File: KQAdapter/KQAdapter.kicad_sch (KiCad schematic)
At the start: 3 parts

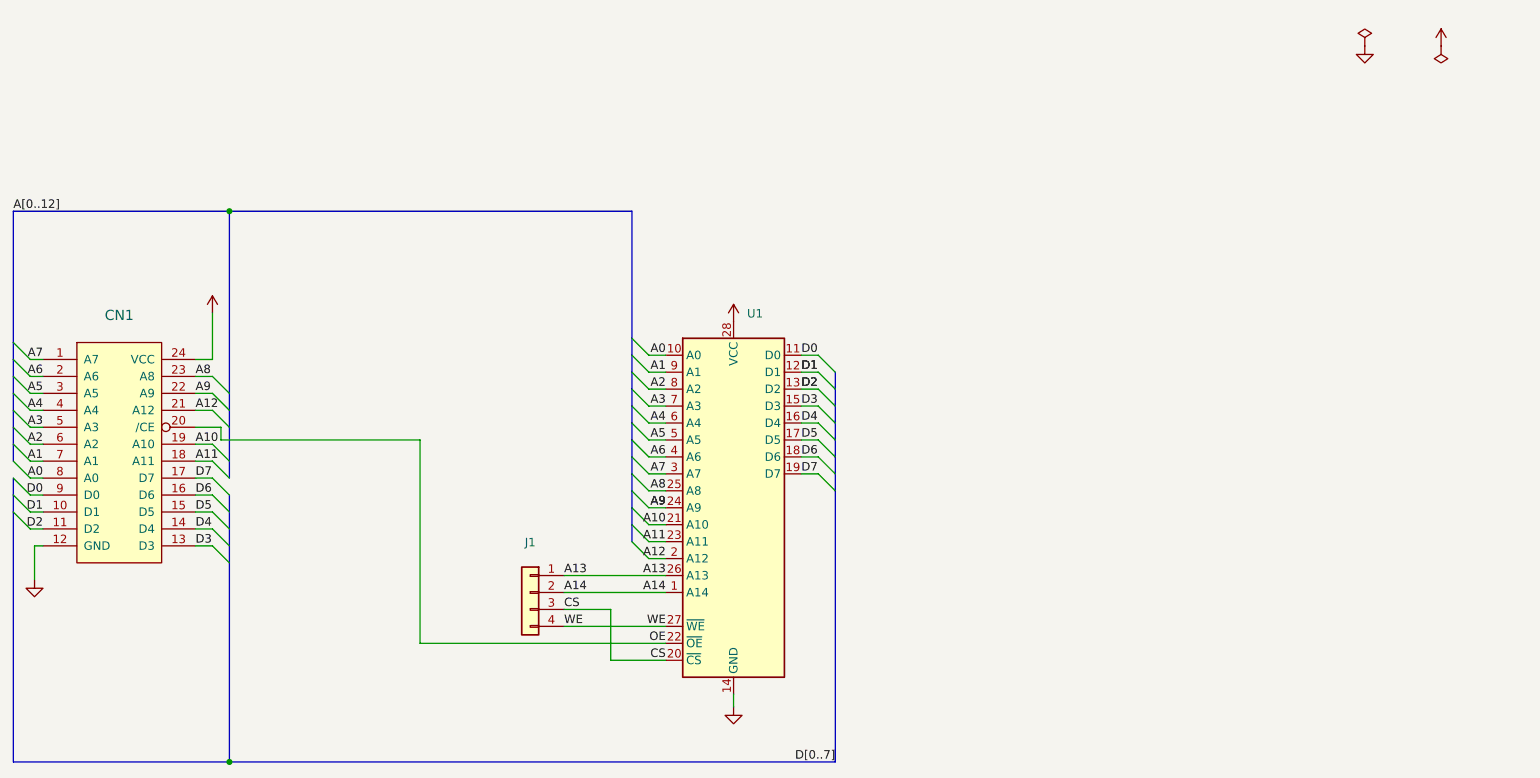
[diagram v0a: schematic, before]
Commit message: Added license information.
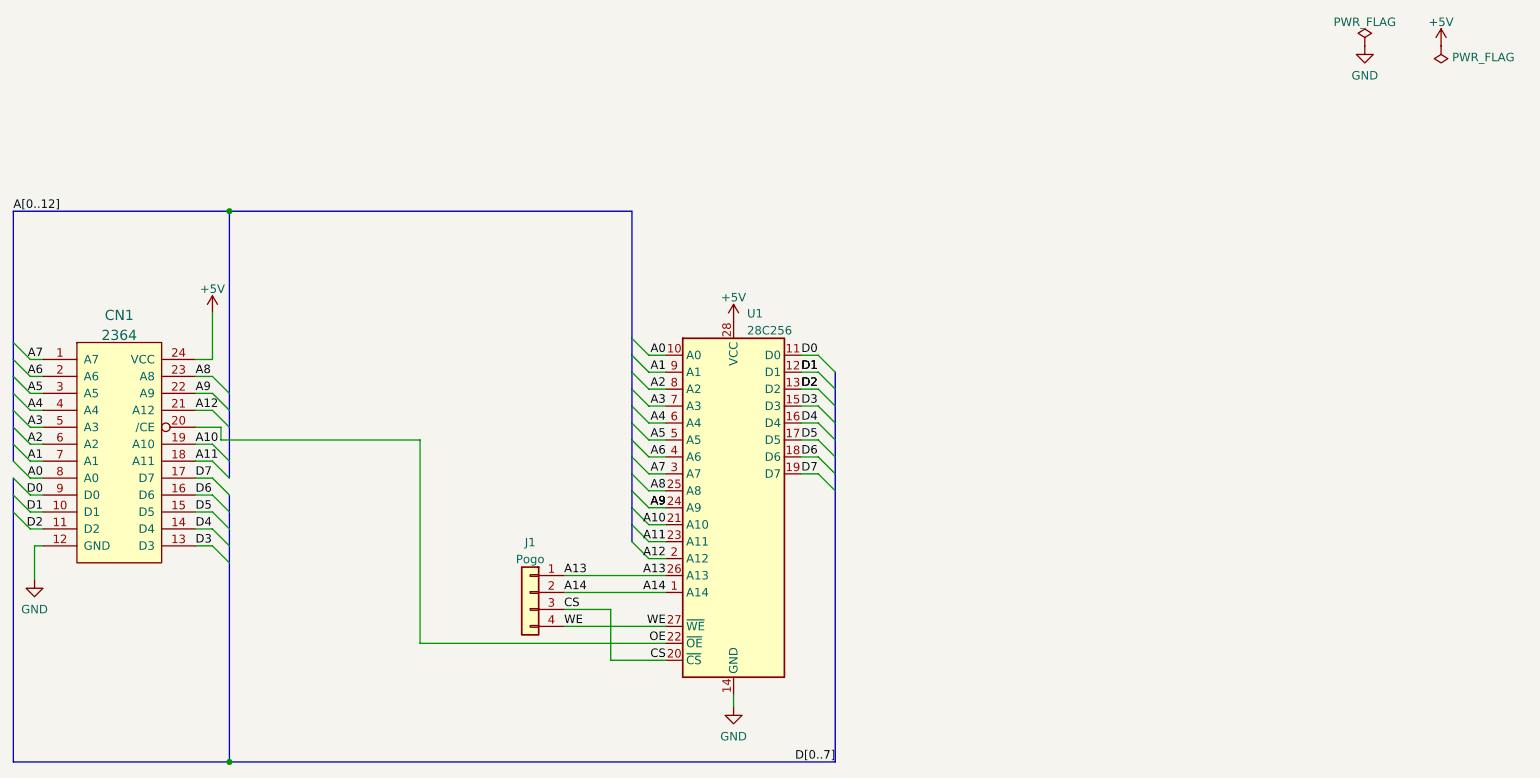
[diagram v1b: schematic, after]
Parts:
- CN1: value (none) -> 2364; footprint (none) -> Package_DIP:DIP-24_W15.24mm_Socket
- J1: value (none) -> Pogo; footprint (none) -> Connector_PinHeader_2.54mm:PinHeader_1x04_P2.54mm_Vertical
- U1: value (none) -> 28C256; footprint (none) -> Package_DIP:DIP-28_W15.24mm
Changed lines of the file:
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@@
   (title_block
     (title "KERNALquattro Adapter")
+    (date "2022-05-02")
     (rev "1")
     (company "www.hackup.net")
+    (comment 1 "Creative Commons Attribution-NonCommercial-ShareAlike 4.0 International License.")
+    (comment 2 "This work is licensed under a")
   )
   (junction (at 85.725 48.26) (diameter 0) (color 0 0 0 0)
@@
       (effects (font (size 1.27 1.27)) hide)
     )
-    (property "Value" "" (id 1) (at 268.986 25.1988 0)
+    (property "Value" "PWR_FLAG" (id 1) (at 268.986 25.1988 0)
       (effects (font (size 1.27 1.27)) (justify right))
     )
@@
       (effects (font (size 1.27 1.27)) hide)
     )
-    (property "Value" "" (id 1) (at 255.905 27.9384 0))
+    (property "Value" "GND" (id 1) (at 255.905 27.9384 0))
     (property "Footprint" "" (id 2) (at 255.905 23.495 0)
       (effects (font (size 1.27 1.27)) hide)
@@
       (effects (font (size 1.27 1.27)) hide)
     )
-    (property "Value" "" (id 1) (at 255.905 19.9192 0))
+    (property "Value" "PWR_FLAG" (id 1) (at 255.905 19.9192 0))
     (property "Footprint" "" (id 2) (at 255.905 23.495 0)
       (effects (font (size 1.27 1.27)) hide)
@@
     (in_bom yes) (on_board yes) (fields_autoplaced)
     (property "Reference" "J1" (id 0) (at 130.81 97.9002 0))
-    (property "Value" "" (id 1) (at 130.81 100.4371 0))
-    (property "Footprint" "" (id 2) (at 130.81 105.41 0)
+    (property "Value" "Pogo" (id 1) (at 130.81 100.4371 0))
+    (property "Footprint" "Connector_PinHeader_2.54mm:PinHeader_1x04_P2.54mm_Vertical" (id 2) (at 130.81 105.41 0)
       (effects (font (size 1.27 1.27)) hide)
     )
@@
       (effects (font (size 1.27 1.27)) hide)
     )
-    (property "Value" "" (id 1) (at 161.29 61.1942 0))
+    (property "Value" "+5V" (id 1) (at 161.29 61.1942 0))
     (property "Footprint" "" (id 2) (at 161.29 64.77 0)
       (effects (font (size 1.27 1.27)) hide)
@@
       (effects (font (size 1.27 1.27)) hide)
     )
-    (property "Value" "" (id 1) (at 161.29 126.9984 0))
+    (property "Value" "GND" (id 1) (at 161.29 126.9984 0))
     (property "Footprint" "" (id 2) (at 161.29 122.555 0)
       (effects (font (size 1.27 1.27)) hide)
@@
       (effects (font (size 1.27 1.27)) hide)
     )
-    (property "Value" "" (id 1) (at 83.185 59.9242 0))
+    (property "Value" "+5V" (id 1) (at 83.185 59.9242 0))
     (property "Footprint" "" (id 2) (at 83.185 63.5 0)
       (effects (font (size 1.27 1.27)) hide)
@@
       (effects (font (size 1.27 1.27)) (justify left))
     )
-    (property "Value" "" (id 1) (at 163.3094 66.1471 0)
+    (property "Value" "28C256" (id 1) (at 163.3094 66.1471 0)
       (effects (font (size 1.27 1.27)) (justify left))
     )
-    (property "Footprint" "" (id 2) (at 161.29 92.71 0)
+    (property "Footprint" "Package_DIP:DIP-28_W15.24mm" (id 2) (at 161.29 92.71 0)
       (effects (font (size 1.27 1.27)) hide)
     )
@@
       (effects (font (size 1.524 1.524)))
     )
-    (property "Value" "" (id 1) (at 69.215 66.8543 0)
+    (property "Value" "2364" (id 1) (at 69.215 66.8543 0)
       (effects (font (size 1.524 1.524)))
     )
-    (property "Footprint" "" (id 2) (at 69.215 66.675 0)
+    (property "Footprint" "Package_DIP:DIP-24_W15.24mm_Socket" (id 2) (at 69.215 66.675 0)
       (effects (font (size 1.524 1.524)) hide)
     )
@@
       (effects (font (size 1.27 1.27)) hide)
     )
-    (property "Value" "" (id 1) (at 56.515 107.9484 0))
+    (property "Value" "GND" (id 1) (at 56.515 107.9484 0))
     (property "Footprint" "" (id 2) (at 56.515 103.505 0)
       (effects (font (size 1.27 1.27)) hide)
@@
       (effects (font (size 1.27 1.27)) hide)
     )
-    (property "Value" "" (id 1) (at 267.335 19.9192 0))
+    (property "Value" "+5V" (id 1) (at 267.335 19.9192 0))
     (property "Footprint" "" (id 2) (at 267.335 23.495 0)
       (effects (font (size 1.27 1.27)) hide)
